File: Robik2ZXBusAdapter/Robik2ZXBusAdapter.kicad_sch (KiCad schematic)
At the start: 8 parts, among them Q1 BC558, Q2 BC558, U1 RobikBUS

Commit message: fixed issues
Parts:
- removed C1, C2: 220, Capacitor_THT:C_Disc_D3.4mm_W2.1mm_P2.50mm, symbol Device:C
- removed Q1, Q2: BC558, Package_TO_SOT_THT:TO-92_Inline, symbol Transistor_BJT:BC558
- added Q1, Q2: BC547, Package_TO_SOT_THT:TO-92_Inline_Wide, symbol Transistor_BJT:BC547
- added R3: 1K, Resistor_THT:R_Axial_DIN0204_L3.6mm_D1.6mm_P5.08mm_Vertical, symbol Device:R
- U1: footprint RobikBUS:RobikBUS -> RobikBUS:RobikBUS_VERT
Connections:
- net +5V: now also Q1.1 (C), Q2.1 (C)
- net GND: now also R3.2
- net /ROMCS: now also R3.1
- net at U1.A30 (/CSROM0): now also Q1.3 (E)
- net at U1.A31 (/CSROM1): now also Q2.3 (E)
- net at R1.1: now also Q1.2 (B)
- net at R2.1: now also Q2.2 (B)
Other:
- note added: "Top Bottom"
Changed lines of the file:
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@@
 (kicad_sch (version 20230121) (generator eeschema)
   (paper "A4")
-  (junction (at 114.3 138.43) (diameter 0) (color 0 0 0 0)
-  )
   (junction (at 90.17 129.54) (diameter 0) (color 0 0 0 0)
-  )
-  (junction (at 114.3 127) (diameter 0) (color 0 0 0 0)
-  )
-  (junction (at 106.68 119.38) (diameter 0) (color 0 0 0 0)
   )
   (no_connect (at 204.47 53.34))
@@
   (no_connect (at 204.47 114.3))
   (no_connect (at 121.92 81.28))
-  (wire (pts (xy 114.3 130.81) (xy 114.3 127))
-    (stroke (width 0) (type default))
-  )
   (wire (pts (xy 100.33 127) (xy 114.3 127))
     (stroke (width 0) (type default))
   )
-  (wire (pts (xy 90.17 129.54) (xy 90.17 135.89))
+  (wire (pts (xy 90.17 129.54) (xy 90.17 138.43))
     (stroke (width 0) (type default))
   )
@@
     (stroke (width 0) (type default))
   )
+  (wire (pts (xy 100.33 137.16) (xy 100.33 138.43))
+    (stroke (width 0) (type default))
+  )
   (wire (pts (xy 87.63 107.95) (xy 92.71 107.95))
     (stroke (width 0) (type default))
@@
     (stroke (width 0) (type default))
   )
-  (wire (pts (xy 106.68 138.43) (xy 114.3 138.43))
+  (wire (pts (xy 100.33 138.43) (xy 120.65 138.43))
     (stroke (width 0) (type default))
   )
@@
     (stroke (width 0) (type default))
   )
-  (wire (pts (xy 106.68 119.38) (xy 106.68 130.81))
-    (stroke (width 0) (type default))
-  )
   (wire (pts (xy 232.41 58.42) (xy 232.41 60.96))
     (stroke (width 0) (type default))
   )
-  (wire (pts (xy 120.65 138.43) (xy 114.3 138.43))
-    (stroke (width 0) (type default))
-  )
   (wire (pts (xy 121.92 124.46) (xy 120.65 124.46))
     (stroke (width 0) (type default))
@@
     (stroke (width 0) (type default))
   )
+  (wire (pts (xy 90.17 129.54) (xy 100.33 129.54))
+    (stroke (width 0) (type default))
+  )
+  (text "Top         Bottom" (at 209.55 43.18 0)
+    (effects (font (size 1.27 1.27)) (justify left bottom))
+  )
   (label "A1" (at 232.41 68.58 0) (fields_autoplaced)
     (effects (font (size 1.27 1.27)) (justify left bottom))
@@
     (effects (font (size 1.27 1.27)) (justify left bottom))
   )
-  (label "{slash}ROMCS" (at 90.17 135.89 0) (fields_autoplaced)
+  (label "{slash}ROMCS" (at 90.17 138.43 0) (fields_autoplaced)
     (effects (font (size 1.27 1.27)) (justify left bottom))
   )
@@
   (label "A14" (at 232.41 45.72 0) (fields_autoplaced)
     (effects (font (size 1.27 1.27)) (justify left bottom))
-  )
-  (symbol (lib_id "Device:C") (at 106.68 134.62 0) (unit 1)
-    (in_bom yes) (on_board yes) (dnp no)
-    (property "Reference" "C2" (at 106.68 132.08 0)
-      (effects (font (size 1.27 1.27)) (justify left))
-    )
-    (property "Value" "220" (at 101.6 132.08 0)
-      (effects (font (size 1.27 1.27)) (justify left))
-    )
-    (property "Footprint" "Capacitor_THT:C_Disc_D3.4mm_W2.1mm_P2.50mm" (at 107.6452 138.43 0)
-      (effects (font (size 1.27 1.27)) hide)
-    )
-    (property "Datasheet" "~" (at 106.68 134.62 0)
-      (effects (font (size 1.27 1.27)) hide)
-    )
-    (pin "1")
-    (pin "2")
-    (instances
-      (project "Robik2ZXBusAdapter"
-        (path "/ddb00022-6bca-4b91-ae7b-81ca3e51df78"
-          (reference "C2") (unit 1)
-        )
-      )
-    )
   )
   (symbol (lib_id "robikbus:RobikBUS") (at 109.22 128.27 0) (unit 1)
@@
       (effects (font (size 1.27 1.27)))
     )
-    (property "Footprint" "RobikBUS:RobikBUS" (at 118.11 125.73 0)
+    (property "Footprint" "RobikBUS:RobikBUS_VERT" (at 118.11 125.73 0)
       (effects (font (size 1.27 1.27)) hide)
     )
@@
     )
   )
-  (symbol (lib_id "Transistor_BJT:BC558") (at 97.79 121.92 0) (unit 1)
-    (in_bom yes) (on_board yes) (dnp no)
-    (property "Reference" "Q2" (at 102.87 120.65 0)
-      (effects (font (size 1.27 1.27)) (justify left))
-    )
-    (property "Value" "BC558" (at 90.17 119.38 0)
-      (effects (font (size 1.27 1.27)) (justify left))
-    )
-    (property "Footprint" "Package_TO_SOT_THT:TO-92_Inline" (at 102.87 123.825 0)
+  (symbol (lib_id "Transistor_BJT:BC547") (at 97.79 107.95 0) (unit 1)
+    (in_bom yes) (on_board yes) (dnp no) (fields_autoplaced)
+    (property "Reference" "Q1" (at 102.87 106.68 0)
+      (effects (font (size 1.27 1.27)) (justify left))
+    )
+    (property "Value" "BC547" (at 102.87 109.22 0)
+      (effects (font (size 1.27 1.27)) (justify left))
+    )
+    (property "Footprint" "Package_TO_SOT_THT:TO-92_Inline_Wide" (at 102.87 109.855 0)
       (effects (font (size 1.27 1.27) italic) (justify left) hide)
     )
-    (property "Datasheet" "https://www.onsemi.com/pub/Collateral/BC556BTA-D.pdf" (at 97.79 121.92 0)
-      (effects (font (size 1.27 1.27)) (justify left) hide)
-    )
-    (pin "1")
-    (pin "2")
-    (pin "3")
-    (instances
-      (project "Robik2ZXBusAdapter"
-        (path "/ddb00022-6bca-4b91-ae7b-81ca3e51df78"
-          (reference "Q2") (unit 1)
-        )
-      )
-    )
-  )
-  (symbol (lib_id "Device:C") (at 114.3 134.62 0) (unit 1)
-    (in_bom yes) (on_board yes) (dnp no)
-    (property "Reference" "C1" (at 111.76 132.08 0)
-      (effects (font (size 1.27 1.27)) (justify left))
-    )
-    (property "Value" "220" (at 115.57 132.08 0)
-      (effects (font (size 1.27 1.27)) (justify left))
-    )
-    (property "Footprint" "Capacitor_THT:C_Disc_D3.4mm_W2.1mm_P2.50mm" (at 115.2652 138.43 0)
-      (effects (font (size 1.27 1.27)) hide)
-    )
-    (property "Datasheet" "~" (at 114.3 134.62 0)
-      (effects (font (size 1.27 1.27)) hide)
-    )
-    (pin "1")
-    (pin "2")
-    (instances
-      (project "Robik2ZXBusAdapter"
-        (path "/ddb00022-6bca-4b91-ae7b-81ca3e51df78"
-          (reference "C1") (unit 1)
-        )
-      )
-    )
-  )
-  (symbol (lib_id "Transistor_BJT:BC558") (at 97.79 107.95 0) (unit 1)
-    (in_bom yes) (on_board yes) (dnp no)
-    (property "Reference" "Q1" (at 102.87 106.68 0)
-      (effects (font (size 1.27 1.27)) (justify left))
-    )
-    (property "Value" "BC558" (at 90.17 105.41 0)
-      (effects (font (size 1.27 1.27)) (justify left))
-    )
-    (property "Footprint" "Package_TO_SOT_THT:TO-92_Inline" (at 102.87 109.855 0)
-      (effects (font (size 1.27 1.27) italic) (justify left) hide)
-    )
-    (property "Datasheet" "https://www.onsemi.com/pub/Collateral/BC556BTA-D.pdf" (at 97.79 107.95 0)
+    (property "Datasheet" "https://www.onsemi.com/pub/Collateral/BC550-D.pdf" (at 97.79 107.95 0)
       (effects (font (size 1.27 1.27)) (justify left) hide)
     )
@@
         )
       )
+    )
+  )
+  (symbol (lib_id "Device:R") (at 100.33 133.35 0) (unit 1)
+    (in_bom yes) (on_board yes) (dnp no) (fields_autoplaced)
+    (property "Reference" "R3" (at 102.87 132.08 0)
+      (effects (font (size 1.27 1.27)) (justify left))
+    )
+    (property "Value" "1K" (at 102.87 134.62 0)
+      (effects (font (size 1.27 1.27)) (justify left))
+    )
+    (property "Footprint" "Resistor_THT:R_Axial_DIN0204_L3.6mm_D1.6mm_P5.08mm_Vertical" (at 98.552 133.35 90)
+      (effects (font (size 1.27 1.27)) hide)
+    )
+    (property "Datasheet" "~" (at 100.33 133.35 0)
+      (effects (font (size 1.27 1.27)) hide)
+    )
+    (pin "1")
+    (pin "2")
+    (instances
+      (project "Robik2ZXBusAdapter"
+        (path "/ddb00022-6bca-4b91-ae7b-81ca3e51df78"
+          (reference "R3") (unit 1)
+        )
+      )
+    )
+  )
+  (symbol (lib_id "Transistor_BJT:BC547") (at 97.79 121.92 0) (unit 1)
+    (in_bom yes) (on_board yes) (dnp no) (fields_autoplaced)
+    (property "Reference" "Q2" (at 102.87 120.65 0)
+      (effects (font (size 1.27 1.27)) (justify left))
+    )
+    (property "Value" "BC547" (at 102.87 123.19 0)
+      (effects (font (size 1.27 1.27)) (justify left))
+    )
+    (property "Footprint" "Package_TO_SOT_THT:TO-92_Inline_Wide" (at 102.87 123.825 0)
+      (effects (font (size 1.27 1.27) italic) (justify left) hide)
+    )
+    (property "Datasheet" "https://www.onsemi.com/pub/Collateral/BC550-D.pdf" (at 97.79 121.92 0)
+      (effects (font (size 1.27 1.27)) (justify left) hide)
+    )
+    (pin "1")
+    (pin "2")
+    (pin "3")
+    (instances
+      (project "Robik2ZXBusAdapter"
+        (path "/ddb00022-6bca-4b91-ae7b-81ca3e51df78"
+          (reference "Q2") (unit 1)
+        )
+      )

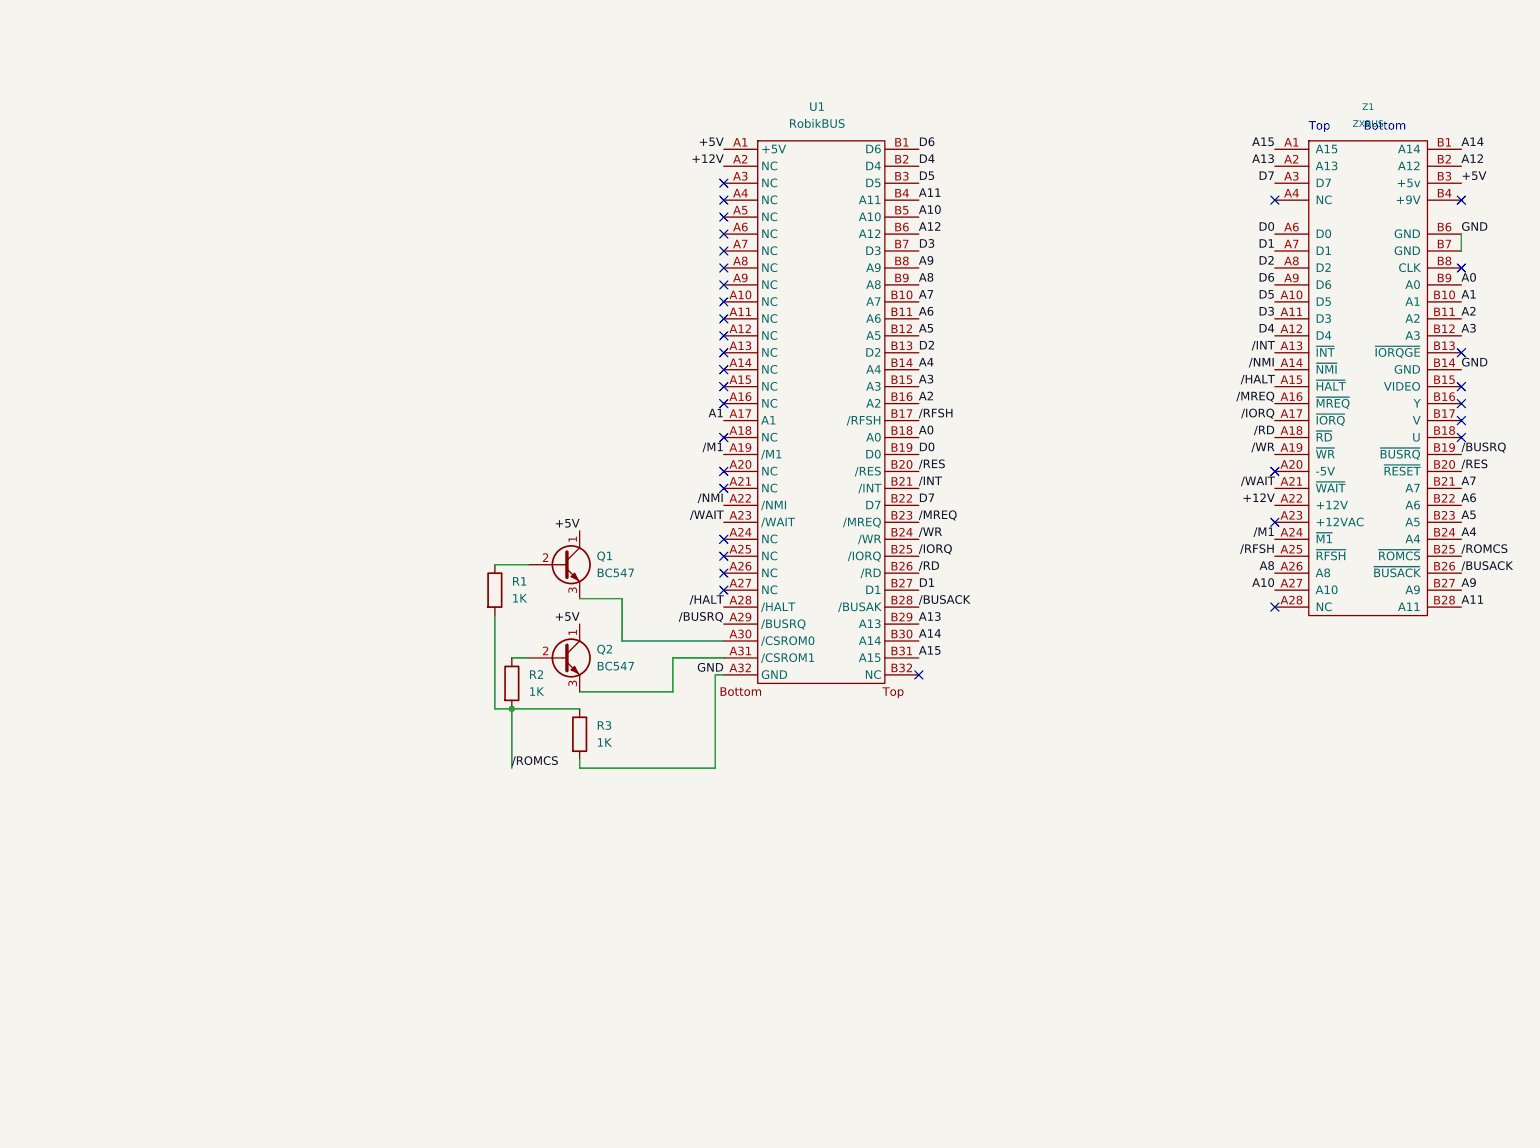
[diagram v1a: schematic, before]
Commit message: added optional rom selector to adapter
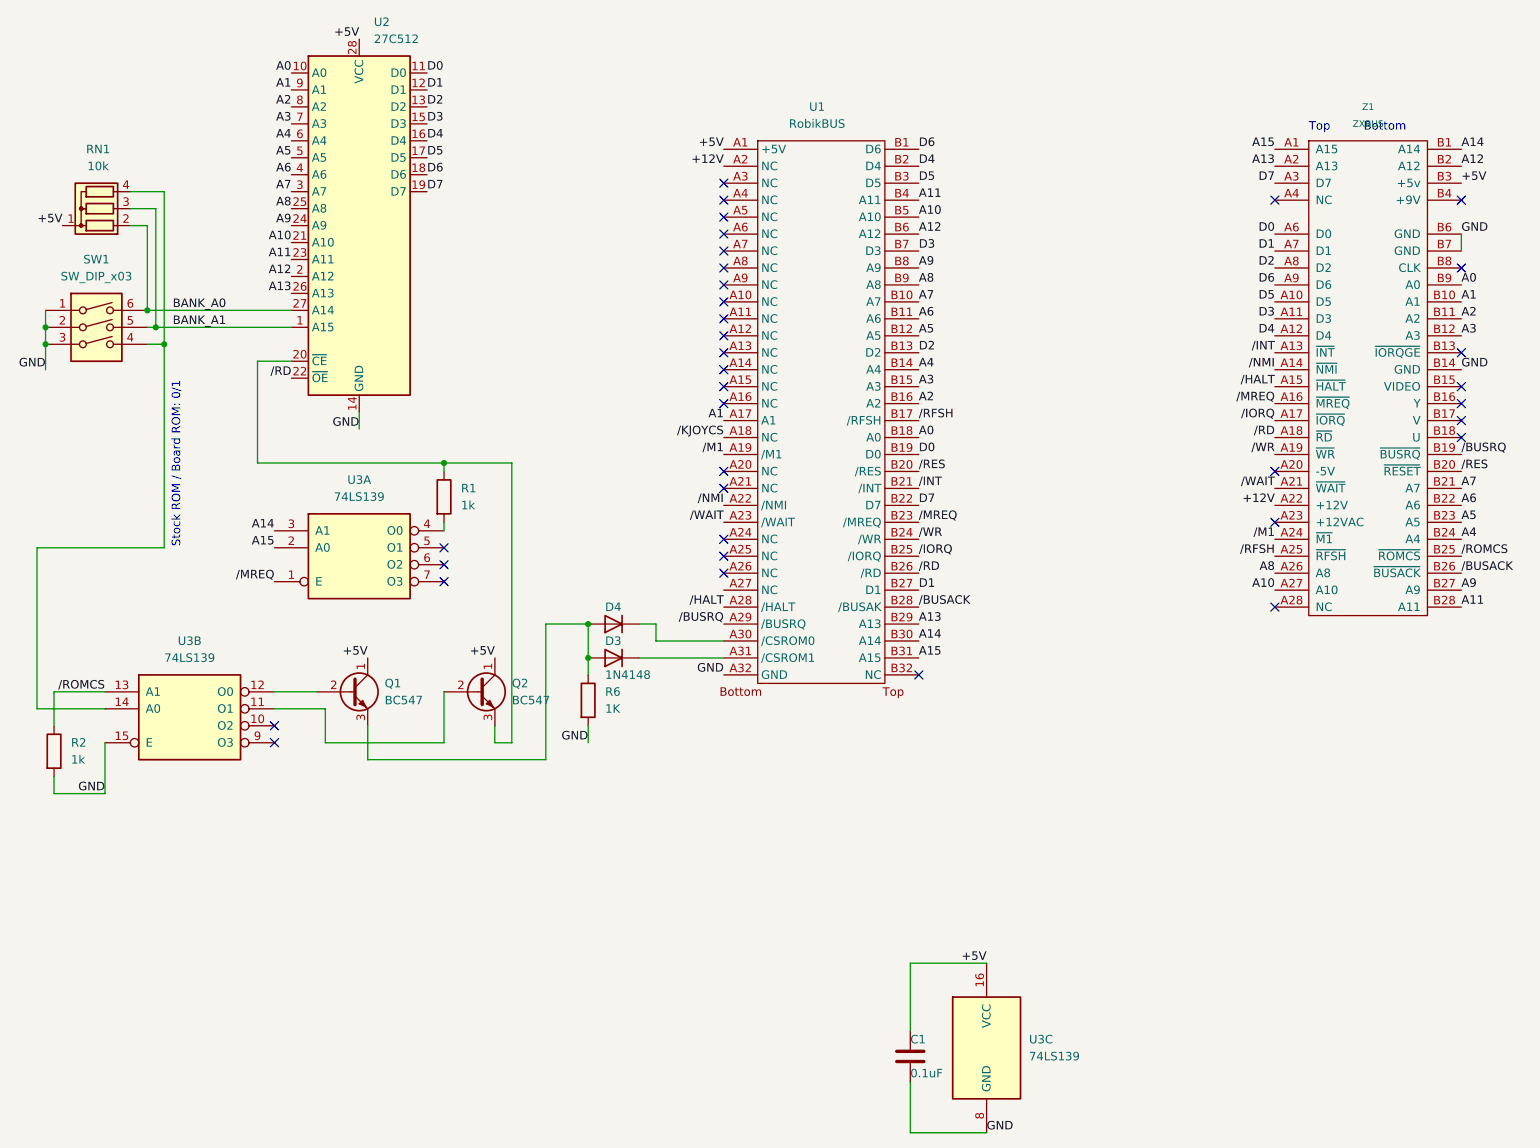
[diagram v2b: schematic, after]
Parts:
- removed R3: 1K, Resistor_THT:R_Axial_DIN0204_L3.6mm_D1.6mm_P5.08mm_Vertical, symbol Device:R
- added C1: 0.1uF, symbol Device:C
- added D3, D4: 1N4148, Diode_THT:D_DO-35_SOD27_P7.62mm_Horizontal, symbol Diode:1N4148
- added R6: 1K, Resistor_THT:R_Axial_DIN0204_L3.6mm_D1.6mm_P5.08mm_Vertical, symbol Device:R
- added RN1: 10k, Resistor_THT:R_Array_SIP4, symbol Device:R_Network03
- added SW1: SW_DIP_x03, symbol Switch:SW_DIP_x03
- added U2: 27C512, Package_DIP:DIP-28_W15.24mm, symbol Memory_EPROM:27C512
- added U3: 74LS139, symbol 74xx:74LS139
- Q1, Q2: footprint Package_TO_SOT_THT:TO-92_Inline_Wide -> Package_TO_SOT_THT:TO-92_Inline
- R1, R2: value 1K -> 1k; footprint Resistor_THT:R_Axial_DIN0204_L3.6mm_D1.6mm_P5.08mm_Vertical -> (none)
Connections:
- net +5V: now also C1.1, RN1.1 (common), U2.28 (VCC), U3.16 (VCC)
- net A0: now also U2.10 (A0)
- net A1: now also U2.9 (A1)
- net A10: now also U2.21 (A10)
- net A11: now also U2.23 (A11)
- net A12: now also U2.2 (A12)
- net A13: now also U2.26 (A13)
- net A14: now also U3.3 (A1)
- net A15: now also U3.2 (A0)
- net A2: now also U2.8 (A2)
- net A3: now also U2.7 (A3)
- net A4: now also U2.6 (A4)
- net A5: now also U2.5 (A5)
- net A6: now also U2.4 (A6)
- net A7: now also U2.3 (A7)
- net A8: now also U2.25 (A8)
- net A9: now also U2.24 (A9)
- net D0: now also U2.11 (D0)
- net D1: now also U2.12 (D1)
- net D2: now also U2.13 (D2)
- net D3: now also U2.15 (D3)
- net D4: now also U2.16 (D4)
- net D5: now also U2.17 (D5)
- net D6: now also U2.18 (D6)
- net D7: now also U2.19 (D7)
- net GND: now also R2.2, C1.2, R6.2, SW1.1, SW1.2, SW1.3, U2.14 (GND), U3.15 (E), U3.8 (GND)
- net /MREQ: now also U3.1 (E)
- net /RD: now also U2.22 (~{OE})
- net /ROMCS: now also R2.1, U3.13 (A1); no longer R1.2, R2.2
- net /KJOYCS: now reaches U1.A18 (NC)
- net at U1.A30 (/CSROM0): now also D4.1 (K); no longer Q1.3 (E)
- net at Q2.3 (E): now also R1.1, U2.20 (~{CE}); no longer U1.A31 (/CSROM1)
- net at Q1.2 (B): now also U3.12 (O0); no longer R1.1
- net at Q2.2 (B): now also U3.11 (O1); no longer R2.1
- new net: R1.2, U3.4 (O0)
- new net: D3.1 (K), U1.A31 (/CSROM1)
- new net: D3.2 (A), D4.2 (A), Q1.3 (E), R6.1
- new net: RN1.4 (R3), SW1.4, U3.14 (A0)
- new net BANK_A0: RN1.2 (R1), SW1.6, U2.27 (A14)
- new net BANK_A1: RN1.3 (R2), SW1.5, U2.1 (A15)
- no-connect marks 33 -> 36
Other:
- note added: "Stock ROM / Board ROM: 0/1"

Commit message: robik bus changes
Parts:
- C1: footprint (none) -> Capacitor_THT:C_Disc_D4.7mm_W2.5mm_P5.00mm
- Q1, Q2: footprint Package_TO_SOT_THT:TO-92_Inline -> Package_TO_SOT_THT:TO-92_Inline_Wide
- R1, R2: footprint (none) -> Resistor_THT:R_Axial_DIN0204_L3.6mm_D1.6mm_P5.08mm_Vertical
- SW1: footprint (none) -> Package_DIP:DIP-6_W7.62mm
- U3: footprint (none) -> Package_DIP:DIP-16_W7.62mm
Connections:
- net /KJOYCS: now also Z1.A28 (NC)
- no-connect marks 36 -> 35
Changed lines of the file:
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@@
   (no_connect (at 204.47 93.98))
   (no_connect (at 54.61 132.08))
-  (no_connect (at 204.47 114.3))
   (no_connect (at 121.92 81.28))
   (wire (pts (xy 68.58 132.08) (xy 68.58 137.16))
@@
   (label "A1" (at 232.41 68.58 0) (fields_autoplaced)
     (effects (font (size 1.27 1.27)) (justify left bottom))
+  )
+  (label "{slash}KJOYCS" (at 204.47 114.3 180) (fields_autoplaced)
+    (effects (font (size 1.27 1.27)) (justify right bottom))
   )
   (label "{slash}HALT" (at 204.47 81.28 180) (fields_autoplaced)
@@
       (effects (font (size 1.27 1.27)) (justify left))
     )
-    (property "Footprint" "" (at 78.232 97.79 90)
+    (property "Footprint" "Resistor_THT:R_Axial_DIN0204_L3.6mm_D1.6mm_P5.08mm_Vertical" (at 78.232 97.79 90)
       (effects (font (size 1.27 1.27)) hide)
     )
@@
       (effects (font (size 1.27 1.27)) (justify left))
     )
-    (property "Footprint" "Package_TO_SOT_THT:TO-92_Inline" (at 90.17 128.905 0)
+    (property "Footprint" "Package_TO_SOT_THT:TO-92_Inline_Wide" (at 90.17 128.905 0)
       (effects (font (size 1.27 1.27) italic) (justify left) hide)
     )
@@
       (effects (font (size 1.27 1.27)) (justify left))
     )
-    (property "Footprint" "" (at 19.812 135.89 90)
+    (property "Footprint" "Resistor_THT:R_Axial_DIN0204_L3.6mm_D1.6mm_P5.08mm_Vertical" (at 19.812 135.89 90)
       (effects (font (size 1.27 1.27)) hide)
     )
@@
       (effects (font (size 1.27 1.27)))
     )
-    (property "Footprint" "" (at 67.31 105.41 0)
+    (property "Footprint" "Package_DIP:DIP-16_W7.62mm" (at 67.31 105.41 0)
       (effects (font (size 1.27 1.27)) hide)
     )
@@
       (effects (font (size 1.27 1.27)) (justify left))
     )
-    (property "Footprint" "" (at 150.8252 185.42 0)
+    (property "Footprint" "Capacitor_THT:C_Disc_D4.7mm_W2.5mm_P5.00mm" (at 150.8252 185.42 0)
       (effects (font (size 1.27 1.27)) hide)
     )
@@
       (effects (font (size 1.27 1.27)) (justify left))
     )
-    (property "Footprint" "" (at 161.29 180.34 0)
+    (property "Footprint" "Package_DIP:DIP-16_W7.62mm" (at 161.29 180.34 0)
       (effects (font (size 1.27 1.27)) hide)
     )
@@
       (effects (font (size 1.27 1.27)))
     )
-    (property "Footprint" "" (at 27.94 74.93 0)
+    (property "Footprint" "Package_DIP:DIP-6_W7.62mm" (at 27.94 74.93 0)
       (effects (font (size 1.27 1.27)) hide)
     )
@@
       (effects (font (size 1.27 1.27)) (justify left))
     )
-    (property "Footprint" "Package_TO_SOT_THT:TO-92_Inline" (at 71.12 128.905 0)
+    (property "Footprint" "Package_TO_SOT_THT:TO-92_Inline_Wide" (at 71.12 128.905 0)
       (effects (font (size 1.27 1.27) italic) (justify left) hide)
     )
@@
       (effects (font (size 1.27 1.27)))
     )
-    (property "Footprint" "" (at 41.91 129.54 0)
-      (effects (font (size 1.27 1.27)) hide)
-    )
+    (property "Footprint" "Package_DIP:DIP-16_W7.62mm" (at 41.91 129.54 0)
+      (effects (font (size 1.27 1.27)) hide)
+    )
